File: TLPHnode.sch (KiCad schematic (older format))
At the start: 24 parts, among them P1 Bat, P2 CONN_01X06, SW1 Reset, U1 NCP703, U2 LD39130S, U3 Si7006-A20, U4 ESP-12E, U5 ISL29035

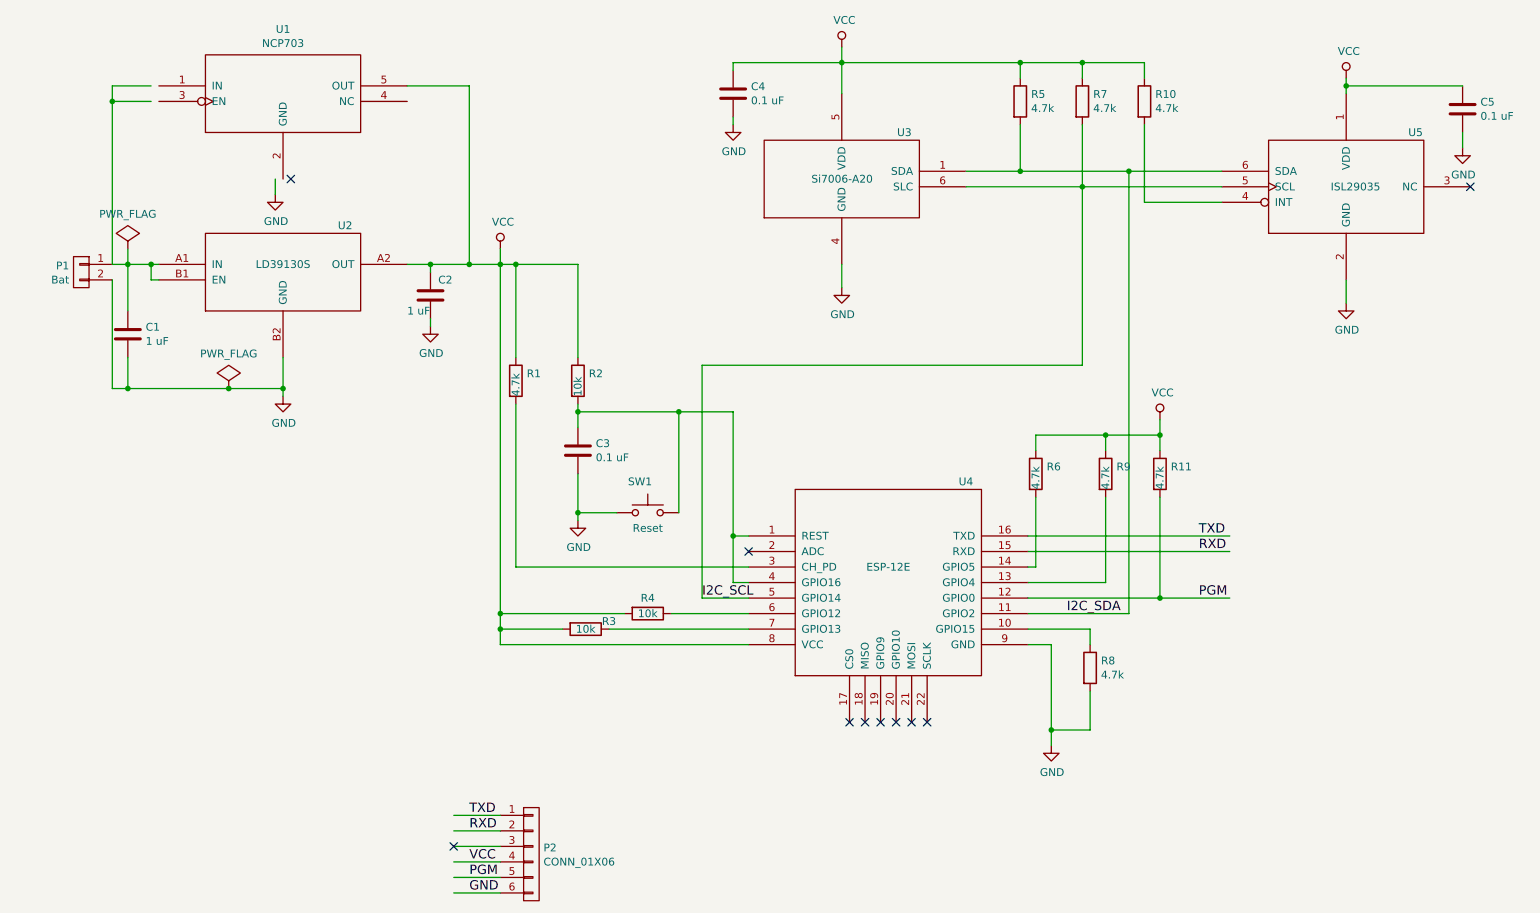
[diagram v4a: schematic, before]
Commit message: Check-point
  - some parts tentatively placed
  - commiting before adding any traces
  - design rules set. OSH 4-layer
On branch master
modified:   TLPHnode-cache.lib
modified:   TLPHnode.kicad_pcb
new file:   TLPHnode.net
modified:   TLPHnode.sch
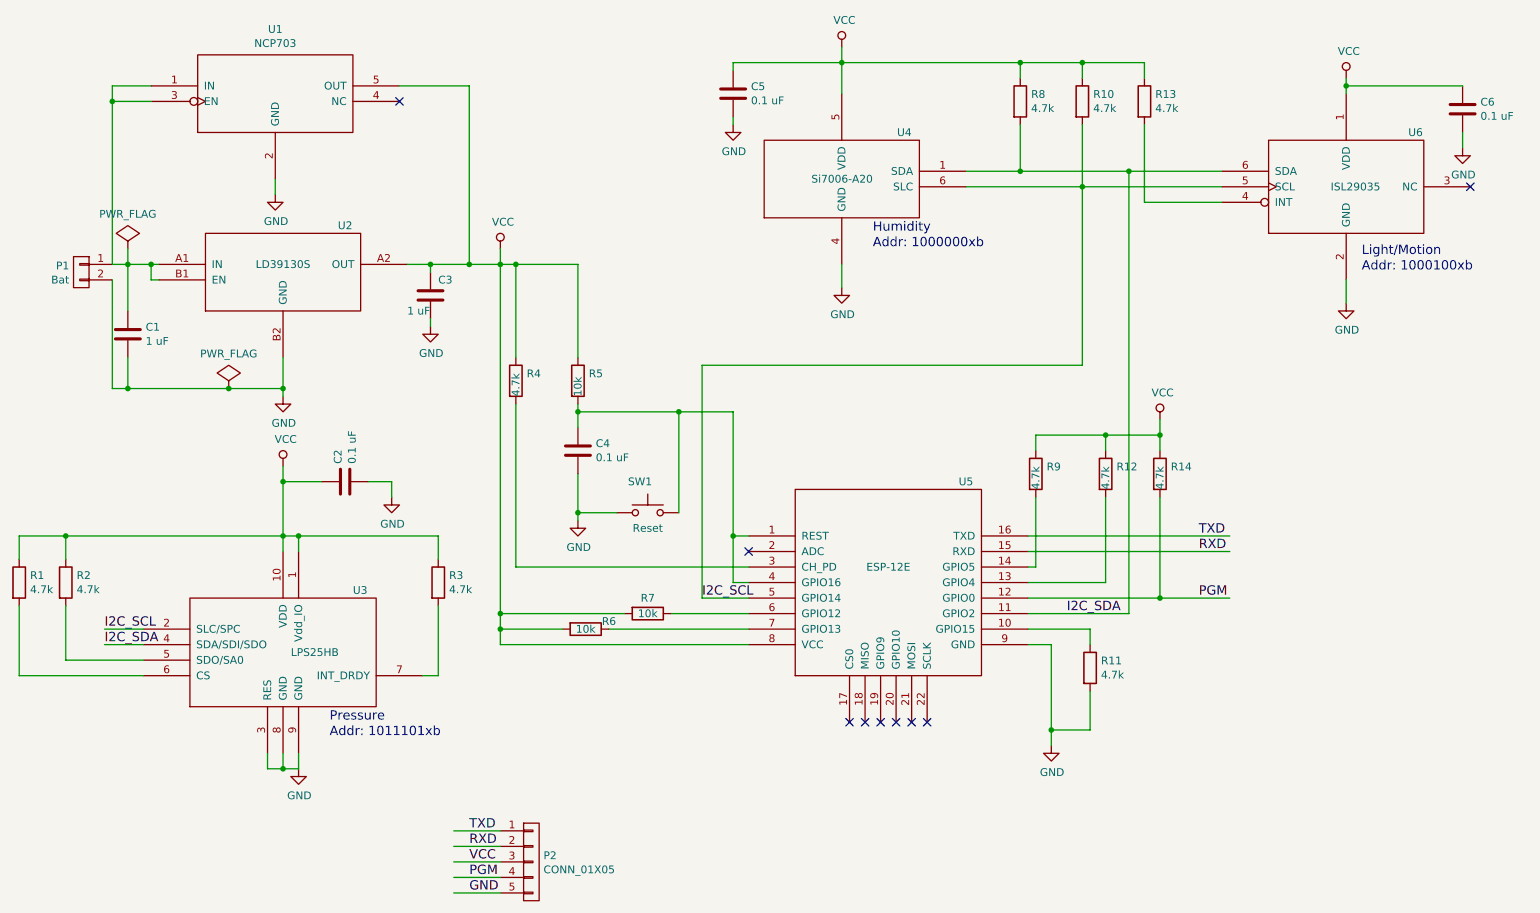
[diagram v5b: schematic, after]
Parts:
- removed P2: CONN_01X06, rockingdlabs:FPC-6-8.43x4.4x2.0mm_Pitch0.5mm, symbol CONN_01X06
- added C2: 0.1 uF, Capacitors_SMD:C_0603, symbol C
- added P2: CONN_01X05, rockingdlabs:FPC_conn-5_8x4.9mm_Pitch0.5mm, symbol CONN_01X05
- added R1, R2, R3: 4.7k, Resistors_SMD:R_0603, symbol R
- added U3: LPS25HB, rockingdlabs:LPS25HB-HLGA-10L-2.5x2.5mm, symbol LPS25HB
- P1: footprint Connectors_JST:JST_PH_S2B-PH-SM4-TB_02x2.00mm_Angled -> rockingdlabs:JST_PH_S2B-PH-SM4-TB_02x2.00mm_Angled
- renumbered C2 to C3, C3 to C4, C4 to C5, C5 to C6, R7 to R10, R8 to R11, R9 to R12, R10 to R13, R11 to R14, R1 to R4, R2 to R5, R3 to R6, R4 to R7, R5 to R8, R6 to R9, U3 to U4, U4 to U5, U5 to U6
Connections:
- wire segments 82 -> 102
- no-connect marks 10 -> 9
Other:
- note added: "Addr: 1000000xb"
- note added: "Addr: 1000100xb"
- note added: "Addr: 1011101xb"
- note added: "Humidity"
- note added: "Light/Motion"
- note added: "Pressure"
- moved on the sheet: U1
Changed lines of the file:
@@
 $EndDescr
 $Comp
-L ESP-12E U4
+L ESP-12E U5
 U 1 1 583B4FA8
 P 6300 4600
-F 0 "U4" H 6800 5250 50  0000 C CNN
+F 0 "U5" H 6800 5250 50  0000 C CNN
 F 1 "ESP-12E" H 6300 4700 50  0000 C CNN
 F 2 "ESP8266:ESP-12E" H 6300 4600 50  0001 C CNN
@@
 $EndComp
 $Comp
-L Si7006-A20 U3
+L Si7006-A20 U4
 U 1 1 583B5CA2
 P 6000 2000
-F 0 "U3" H 6450 2300 50  0000 R CNN
+F 0 "U4" H 6450 2300 50  0000 R CNN
 F 1 "Si7006-A20" H 6200 2000 50  0000 R CNN
 F 2 "rockingdlabs:Si7006_A20-DFN-6" H 6000 2000 50  0001 C CNN
@@
 F 0 "P1" H 1178 2641 50  0000 L CNN
 F 1 "Bat" H 1178 2550 50  0000 L CNN
-F 2 "Connectors_JST:JST_PH_S2B-PH-SM4-TB_02x2.00mm_Angled" H 1100 2600 50  0001 C CNN
+F 2 "rockingdlabs:JST_PH_S2B-PH-SM4-TB_02x2.00mm_Angled" H 1100 2600 50  0001 C CNN
 F 3 "" H 1100 2600 50  0000 C CNN
 	1    1100 2600
 	-1   0    0    -1
-$EndComp
-$Comp
-L CONN_01X06 P2
-U 1 1 583B61FE
-P 4000 6350
-F 0 "P2" H 4078 6391 50  0000 L CNN
-F 1 "CONN_01X06" H 4078 6300 50  0000 L CNN
-F 2 "rockingdlabs:FPC-6-8.43x4.4x2.0mm_Pitch0.5mm" H 4000 6350 50  0001 C CNN
-F 3 "" H 4000 6350 50  0000 C CNN
-	1    4000 6350
-	1    0    0    -1
 $EndComp
 NoConn ~ 5400 4400
@@
 $EndComp
 $Comp
-L R R1
+L R R4
 U 1 1 583B6490
 P 3900 3300
-F 0 "R1" H 3970 3346 50  0000 L CNN
+F 0 "R4" H 3970 3346 50  0000 L CNN
 F 1 "4.7k" V 3900 3200 50  0000 L CNN
 F 2 "Resistors_SMD:R_0603" V 3830 3300 50  0001 C CNN
@@
 $EndComp
 $Comp
-L R R2
+L R R5
 U 1 1 583B6506
 P 4300 3300
-F 0 "R2" H 4370 3346 50  0000 L CNN
+F 0 "R5" H 4370 3346 50  0000 L CNN
 F 1 "10k" V 4300 3200 50  0000 L CNN
 F 2 "Resistors_SMD:R_0603" V 4230 3300 50  0001 C CNN
@@
 $EndComp
 $Comp
-L C C3
+L C C4
 U 1 1 583B653A
 P 4300 3750
-F 0 "C3" H 4415 3796 50  0000 L CNN
+F 0 "C4" H 4415 3796 50  0000 L CNN
 F 1 "0.1 uF" H 4415 3705 50  0000 L CNN
 F 2 "Capacitors_SMD:C_0603" H 4338 3600 50  0001 C CNN
@@
 Text Label 3600 6600 0    60   ~ 0
 GND
+Text Label 3600 6300 0    60   ~ 0
+RXD
 Text Label 3600 6200 0    60   ~ 0
-RXD
-Text Label 3600 6100 0    60   ~ 0
 TXD
 Text Label 8300 4300 0    60   ~ 0
@@
 	3800 6200 3500 6200
 Wire Wire Line
-	3800 6100 3500 6100
-Wire Wire Line
 	3800 6600 3500 6600
 Wire Wire Line
@@
 	6800 2050 8450 2050
 $Comp
-L R R5
+L R R8
 U 1 1 583BB767
 P 7150 1500
-F 0 "R5" H 7220 1546 50  0000 L CNN
+F 0 "R8" H 7220 1546 50  0000 L CNN
 F 1 "4.7k" H 7220 1455 50  0000 L CNN
 F 2 "Resistors_SMD:R_0603" V 7080 1500 50  0001 C CNN
@@
 $EndComp
 $Comp
-L R R7
+L R R10
 U 1 1 583BB7BB
 P 7550 1500
-F 0 "R7" H 7620 1546 50  0000 L CNN
+F 0 "R10" H 7620 1546 50  0000 L CNN
 F 1 "4.7k" H 7620 1455 50  0000 L CNN
 F 2 "Resistors_SMD:R_0603" V 7480 1500 50  0001 C CNN
@@
 $EndComp
 $Comp
-L R R10
+L R R13
 U 1 1 583BB80B
 P 7950 1500
-F 0 "R10" H 8020 1546 50  0000 L CNN
+F 0 "R13" H 8020 1546 50  0000 L CNN
 F 1 "4.7k" H 8020 1455 50  0000 L CNN
 F 2 "Resistors_SMD:R_0603" V 7880 1500 50  0001 C CNN
@@
 I2C_SCL
 $Comp
-L ISL29035 U5
+L ISL29035 U6
 U 1 1 583B526D
 P 9250 2050
-F 0 "U5" H 9650 2400 50  0000 L CNN
+F 0 "U6" H 9650 2400 50  0000 L CNN
 F 1 "ISL29035" H 9150 2050 50  0000 L CNN
 F 2 "rockingdlabs:ISL29035-DFN-6-1.5x1.6mm_Pitch0.5mm" H 8550 1600 50  0001 C CNN
@@
 	7350 5000 7350 5650
 $Comp
-L R R8
+L R R11
 U 1 1 583BC6B1
 P 7600 5150
-F 0 "R8" H 7670 5196 50  0000 L CNN
+F 0 "R11" H 7670 5196 50  0000 L CNN
 F 1 "4.7k" H 7670 5105 50  0000 L CNN
 F 2 "Resistors_SMD:R_0603" V 7530 5150 50  0001 C CNN
@@
 PGM
 $Comp
-L R R3
+L R R6
 U 1 1 583BCA9C
 P 4350 4900
-F 0 "R3" V 4300 5050 50  0000 C CNN
+F 0 "R6" V 4300 5050 50  0000 C CNN
 F 1 "10k" V 4350 4900 50  0000 C CNN
 F 2 "Resistors_SMD:R_0603" V 4280 4900 50  0001 C CNN
@@
 $EndComp
 $Comp
-L R R4
+L R R7
 U 1 1 583BCB48
 P 4750 4800
-F 0 "R4" V 4650 4800 50  0000 C CNN
+F 0 "R7" V 4650 4800 50  0000 C CNN
 F 1 "10k" V 4750 4800 50  0000 C CNN
 F 2 "Resistors_SMD:R_0603" V 4680 4800 50  0001 C CNN
@@
 Connection ~ 3800 4900
 $Comp
-L R R11
+L R R14
 U 1 1 583BD162
 P 8050 3900
-F 0 "R11" H 8120 3946 50  0000 L CNN
+F 0 "R14" H 8120 3946 50  0000 L CNN
 F 1 "4.7k" V 8050 3800 50  0000 L CNN
 F 2 "Resistors_SMD:R_0603" V 7980 3900 50  0001 C CNN
@@
 Connection ~ 8050 4700
 $Comp
-L R R9
+L R R12
 U 1 1 583BD5E7
 P 7700 3900
-F 0 "R9" H 7770 3946 50  0000 L CNN
+F 0 "R12" H 7770 3946 50  0000 L CNN
 F 1 "4.7k" V 7700 3800 50  0000 L CNN
 F 2 "Resistors_SMD:R_0603" V 7630 3900 50  0001 C CNN
@@
 	7200 4600 7700 4600
 $Comp
-L R R6
+L R R9
 U 1 1 583BD73B
 P 7250 3900
-F 0 "R6" H 7320 3946 50  0000 L CNN
+F 0 "R9" H 7320 3946 50  0000 L CNN
 F 1 "4.7k" V 7250 3800 50  0000 L CNN
 F 2 "Resistors_SMD:R_0603" V 7180 3900 50  0001 C CNN
@@
 Connection ~ 7700 3650
 $Comp
-L C C5
+L C C6
 U 1 1 583BE035
 P 10000 1550
-F 0 "C5" H 10115 1596 50  0000 L CNN
+F 0 "C6" H 10115 1596 50  0000 L CNN
 F 1 "0.1 uF" H 10115 1505 50  0000 L CNN
 F 2 "Capacitors_SMD:C_0603" H 10038 1400 50  0001 C CNN
@@
 	10000 1700 10000 1800
 $Comp
-L C C4
+L C C5
 U 1 1 583BE33E
 P 5300 1450
-F 0 "C4" H 5415 1496 50  0000 L CNN
+F 0 "C5" H 5415 1496 50  0000 L CNN
 F 1 "0.1 uF" H 5415 1405 50  0000 L CNN
 F 2 "Capacitors_SMD:C_0603" H 5338 1300 50  0001 C CNN
@@
 Wire Wire Line
 	5300 1300 5300 1250
-Wire Wire Line
-	5300 1600 5300 1650
 $Comp
 L C C1
@@
 $EndComp
 $Comp
-L C C2
+L C C3
 U 1 1 583BE718
 P 3350 2750
-F 0 "C2" H 3400 2850 50  0000 L CNN
+F 0 "C3" H 3400 2850 50  0000 L CNN
 F 1 "1 uF" H 3200 2650 50  0000 L CNN
 F 2 "Capacitors_SMD:C_0603" H 3388 2600 50  0001 C CNN
@@
 	1400 3150 1400 3350
 Connection ~ 1400 3350
-NoConn ~ 3500 6300
 $Comp
 L PWR_FLAG #FLG014
@@
 L NCP703 U1
 U 1 1 58460C40
-P 2400 1450
-F 0 "U1" H 2400 1865 50  0000 C CNN
-F 1 "NCP703" H 2400 1774 50  0000 C CNN
-F 2 "rockingdlabs:NCP703-TSOP-5" H 2400 1450 50  0001 C CNN
-F 3 "DOCUMENTATION" H 2400 1450 50  0001 C CNN
-	1    2400 1450
-	1    0    0    -1
-$EndComp
-NoConn ~ 2450 2000
+P 2350 1450
+F 0 "U1" H 2350 1865 50  0000 C CNN
+F 1 "NCP703" H 2350 1774 50  0000 C CNN
+F 2 "rockingdlabs:NCP703-TSOP-5" H 2350 1450 50  0001 C CNN
+F 3 "DOCUMENTATION" H 2350 1450 50  0001 C CNN
+	1    2350 1450
+	1    0    0    -1
+$EndComp
+NoConn ~ 3150 1500
 Wire Wire Line
 	3600 1400 3600 2550
 Wire Wire Line
-	3200 1400 3600 1400
+	3150 1400 3600 1400
+$Comp
+L CONN_01X05 P2
+U 1 1 58479EF6
+P 4000 6400
+F 0 "P2" H 4078 6441 50  0000 L CNN
+F 1 "CONN_01X05" H 4078 6350 50  0000 L CNN
+F 2 "rockingdlabs:FPC_conn-5_8x4.9mm_Pitch0.5mm" H 4000 6400 50  0001 C CNN
+F 3 "" H 4000 6400 50  0000 C CNN
+	1    4000 6400
+	1    0    0    -1
+$EndComp
+$Comp
+L GND #PWR016
+U 1 1 5847A986
+P 2500 5800
+F 0 "#PWR016" H 2500 5550 50  0001 C CNN
+F 1 "GND" H 2505 5627 50  0000 C CNN
+F 2 "" H 2500 5800 50  0000 C CNN
+F 3 "" H 2500 5800 50  0000 C CNN
+	1    2500 5800
+	1    0    0    -1
+$EndComp
+$Comp
+L VCC #PWR017
+U 1 1 5847AAD6
+P 2400 3850
+F 0 "#PWR017" H 2400 3700 50  0001 C CNN
+F 1 "VCC" H 2417 4023 50  0000 C CNN
+F 2 "" H 2400 3850 50  0000 C CNN
+F 3 "" H 2400 3850 50  0000 C CNN
+	1    2400 3850
+	1    0    0    -1
+$EndComp
+Wire Wire Line
+	2400 3850 2400 4400
+Wire Wire Line
+	2500 5800 2500 5700
+Wire Wire Line
+	2400 5700 2400 5800
+Wire Wire Line
+	2300 5800 2500 5800
+Wire Wire Line
+	2300 5700 2300 5800
+Connection ~ 2400 5800
+Wire Wire Line
+	2500 4400 2500 4300
+Wire Wire Line
+	700  4300 3400 4300
+Connection ~ 2400 4300
+$Comp
+L R R3
+U 1 1 58483449
+P 3400 4600
+F 0 "R3" H 3470 4646 50  0000 L CNN
+F 1 "4.7k" H 3470 4555 50  0000 L CNN
+F 2 "Resistors_SMD:R_0603" V 3330 4600 50  0001 C CNN
+F 3 "" H 3400 4600 50  0000 C CNN
+	1    3400 4600
+	1    0    0    -1
+$EndComp
+Wire Wire Line
+	3300 5200 3400 5200
+Wire Wire Line
+	3400 5200 3400 4750
+Wire Wire Line
+	3400 4300 3400 4450
+Wire Wire Line
+	1500 4900 1250 4900
+Wire Wire Line
+	1500 5000 1250 5000
+Text Label 1250 4900 0    60   ~ 0
+I2C_SCL
+Text Label 1250 5000 0    60   ~ 0
+I2C_SDA
+$Comp
+L R R1
+U 1 1 58483D82
+P 700 4600
+F 0 "R1" H 770 4646 50  0000 L CNN
+F 1 "4.7k" H 770 4555 50  0000 L CNN
+F 2 "Resistors_SMD:R_0603" V 630 4600 50  0001 C CNN
+F 3 "" H 700 4600 50  0000 C CNN
+	1    700  4600
+	1    0    0    -1
+$EndComp
+Wire Wire Line
+	700  4750 700  5200
+Wire Wire Line
+	700  5200 1500 5200
+Wire Wire Line
+	700  4450 700  4300
+$Comp
+L R R2
+U 1 1 58484063
+P 1000 4600
+F 0 "R2" H 1070 4646 50  0000 L CNN
+F 1 "4.7k" H 1070 4555 50  0000 L CNN
+F 2 "Resistors_SMD:R_0603" V 930 4600 50  0001 C CNN
+F 3 "" H 1000 4600 50  0000 C CNN
+	1    1000 4600
+	1    0    0    -1
+$EndComp
+Wire Wire Line
+	1500 5100 1000 5100
+Wire Wire Line
+	1000 5100 1000 4750
+Wire Wire Line
+	1000 4450 1000 4300
+Connection ~ 1000 4300
+Text Notes 2700 5500 0    60   ~ 0
+Pressure
+Text Notes 9350 2500 0    60   ~ 0
+Light/Motion
+Text Notes 6200 2350 0    60   ~ 0
+Humidity
+$Comp
+L C C2
+U 1 1 584846C5
+P 2800 3950
+F 0 "C2" H 2915 3996 50  0000 L CNN
+F 1 "0.1 uF" H 2915 3905 50  0000 L CNN
+F 2 "Capacitors_SMD:C_0603" H 2838 3800 50  0001 C CNN
+F 3 "" H 2800 3950 50  0000 C CNN
+	1    2800 3950
+	0    -1   -1   0
+$EndComp
+$Comp
+L GND #PWR018
+U 1 1 584848C6
+P 3100 4050
+F 0 "#PWR018" H 3100 3800 50  0001 C CNN
+F 1 "GND" H 3105 3877 50  0000 C CNN
+F 2 "" H 3100 4050 50  0000 C CNN
+F 3 "" H 3100 4050 50  0000 C CNN
+	1    3100 4050
+	1    0    0    -1
+$EndComp
+Wire Wire Line
+	2650 3950 2400 3950
+Connection ~ 2400 3950
+Wire Wire Line
+	2950 3950 3100 3950
+Wire Wire Line
+	3100 3950 3100 4050
+Text Notes 2700 5600 0    60   ~ 0
+Addr: 1011101xb
+Text Notes 6200 2450 0    60   ~ 0
+Addr: 1000000xb
+Text Notes 9350 2600 0    60   ~ 0
+Addr: 1000100xb
+Wire Wire Line
+	5300 1600 5300 1650
+$Comp
+L LPS25HB U3
+U 1 1 584A1073
+P 2400 5050
+F 0 "U3" H 2850 5450 50  0000 L CNN
+F 1 "LPS25HB" H 2450 5050 50  0000 L CNN
+F 2 "rockingdlabs:LPS25HB-HLGA-10L-2.5x2.5mm" H 2400 5050 50  0001 C CNN
+F 3 "DOCUMENTATION" H 2400 5050 50  0001 C CNN
+	1    2400 5050
+	1    0    0    -1
+$EndComp
+Connection ~ 2500 4300
 $EndSCHEMATC
